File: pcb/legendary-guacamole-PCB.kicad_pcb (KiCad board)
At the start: 2 copper layers, 46 parts

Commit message: forget to commit
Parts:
- added REF**: XIAO-nRF52840-SMD, XIAO-nRF52840-SMD, F.Cu at (257.1, 59.7)
- B1, D1, D10, D11, D12, D13, D14, D15, D16, D17, D18, D19, D2, D20, D21, D22, D3, D4, D5, D6, D7, D8, D9, JST1, S1, S10, S11, S12, S13, S14, S15, S16, S17, S18, S19, S2, S20, S21, S22, S3, S4, S5, S6, S7, S8, S9: value ~ -> (none)
- moved B1 56.2 mm to (187.5, 57.4)
- moved JST1 54.3 mm to (193.8, 70.9)
- moved D1 48.1 mm to (71.0, 118.4)
- moved D10 48.1 mm to (128.0, 86.7)
- moved D11 48.1 mm to (128.0, 67.7)
- moved D12 48.1 mm to (147.0, 112.0)
- moved D13 48.1 mm to (147.0, 93.0)
- moved D14 48.1 mm to (147.0, 74.0)
- moved D15 48.1 mm to (166.0, 112.0)
- moved D16 48.1 mm to (166.0, 93.0)
- moved D17 48.1 mm to (166.0, 74.0)
- moved D2 48.1 mm to (71.0, 99.4)
- moved D4 48.1 mm to (90.0, 99.4)
- moved D5 48.1 mm to (90.0, 80.4)
- moved D6 48.1 mm to (109.0, 112.0)
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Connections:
- net /BAT_P renamed BAT_P
- net /GND renamed GND
- net /P0 renamed P0
- net /P1 renamed P1
- net /P10 renamed P10
- net /P2 renamed P2
- net /P3 renamed P3
- net /P4 renamed P4
- net /P5 renamed P5
- net /P6 renamed P6
- net /P7 renamed P7
- net /P8 renamed P8
- net /P9 renamed P9
- net /RST renamed RST
- net /index_bottom renamed index_bottom
- net /index_home renamed index_home
- net /index_top renamed index_top
- net /inner_bottom renamed inner_bottom
- net /inner_home renamed inner_home
- net /inner_top renamed inner_top
- net /middle_bottom renamed middle_bottom
- net /middle_home renamed middle_home
- net /middle_top renamed middle_top
- net /outer_bottom renamed outer_bottom
- net /outer_home renamed outer_home
- net /pinky_bottom renamed pinky_bottom
- net /pinky_home renamed pinky_home
- net /pinky_top renamed pinky_top
- net /ring_bottom renamed ring_bottom
- net /ring_home renamed ring_home
- net /ring_top renamed ring_top
- net /thumb_1_row_0 renamed thumb_1_row_0
- net /thumb_1_row_1 renamed thumb_1_row_1
- net /thumb_2_row_0 renamed thumb_2_row_0
- net /thumb_2_row_1 renamed thumb_2_row_1
- net /thumb_3_row_0 renamed thumb_3_row_0
- JST1 pad 11: (no net) -> JST1_1
- JST1 pad 12: (no net) -> JST1_2
- JST1 pad 21: (no net) -> JST1_1
- JST1 pad 22: (no net) -> JST1_2
- JST1 pad 31: (no net) -> JST1_1
- JST1 pad 32: (no net) -> JST1_2
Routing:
- net JST1_2: track 0.00 -> 3.60 mm
- net JST1_1: track 0.00 -> 3.60 mm

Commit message: update pcb with new key layout
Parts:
- added D23: , ComboDiode, F.Cu at (222.1, 143.9)
- added S23: , MX, F.Cu at (224.6, 139.6)
- moved REF** 264.0 mm to (0.00, 0.00)
- moved D18 103.7 mm to (195.0, 60.7), turned to 0 degrees
- moved S18 103.3 mm to (195.0, 55.7), turned to 0 degrees
- moved D12 58.6 mm to (157.0, 54.3)
- moved S12 58.6 mm to (157.0, 49.3)
- moved D15 52.3 mm to (176.0, 60.7)
- moved S15 52.3 mm to (176.0, 55.7)
- moved D3 52.3 mm to (100.0, 67.0)
- moved S3 52.3 mm to (100.0, 62.0)
- moved D6 46.1 mm to (119.0, 67.0)
- moved S6 46.1 mm to (119.0, 62.0)
- moved D9 46.1 mm to (138.0, 60.7)
- moved S9 46.1 mm to (138.0, 55.7)
- moved S22 42.8 mm to (207.7, 121.3), turned to -20 degrees
- moved S20 42.7 mm to (184.3, 116.8), turned to -10 degrees
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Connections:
- D10 pad 1: P7 -> P8
- D10 pad 2: middle_home -> middle_bottom
- D11 pad 1: P6 -> P7
- D11 pad 2: middle_top -> middle_home
- D12 pad 1: P8 -> P6
- D12 pad 2: index_bottom -> middle_top
- D13 pad 1: P7 -> P8
- D13 pad 2: index_home -> index_bottom
- D14 pad 1: P6 -> P7
- D14 pad 2: index_top -> index_home
- D15 pad 1: P8 -> P6
- D15 pad 2: inner_bottom -> index_top
- D16 pad 1: P7 -> P8
- D16 pad 2: inner_home -> inner_bottom
- D17 pad 1: P6 -> P7
- D17 pad 2: inner_top -> inner_home
- D18 pad 1: P10 -> P6
- D18 pad 2: thumb_1_row_0 -> inner_top
- D19 pad 1: P9 -> P10
- D19 pad 2: thumb_1_row_1 -> thumb_1_row_0
- D20 pad 1: P10 -> P9
- D20 pad 2: thumb_2_row_0 -> thumb_1_row_1
- D21 pad 1: P9 -> P10
- D21 pad 2: thumb_2_row_1 -> thumb_2_row_0
- D22 pad 1: P10 -> P9
- D22 pad 2: thumb_3_row_0 -> thumb_2_row_1
- D3 pad 1: P8 -> P6
- D3 pad 2: pinky_bottom -> outer_top
- D4 pad 1: P7 -> P8
- D4 pad 2: pinky_home -> pinky_bottom
- D5 pad 1: P6 -> P7
- D5 pad 2: pinky_top -> pinky_home
- D6 pad 1: P8 -> P6
- D6 pad 2: ring_bottom -> pinky_top
- D7 pad 1: P7 -> P8
- D7 pad 2: ring_home -> ring_bottom
- D8 pad 1: P6 -> P7
- D8 pad 2: ring_top -> ring_home
- D9 pad 1: P8 -> P6
- D9 pad 2: middle_bottom -> ring_top
- S10 pad 2: middle_home -> middle_bottom
- S11 pad 2: middle_top -> middle_home
- S12 pad 1: P4 -> P3
- S12 pad 2: index_bottom -> middle_top
- S13 pad 2: index_home -> index_bottom
- S14 pad 2: index_top -> index_home
- S15 pad 1: P5 -> P4
- S15 pad 2: inner_bottom -> index_top
- S16 pad 2: inner_home -> inner_bottom
- S17 pad 2: inner_top -> inner_home
- S18 pad 1: P3 -> P5
- S18 pad 2: thumb_1_row_0 -> inner_top
- S19 pad 2: thumb_1_row_1 -> thumb_1_row_0
- S20 pad 1: P4 -> P3
- S20 pad 2: thumb_2_row_0 -> thumb_1_row_1
- S21 pad 2: thumb_2_row_1 -> thumb_2_row_0
- S22 pad 1: P5 -> P4
- S22 pad 2: thumb_3_row_0 -> thumb_2_row_1
- S3 pad 1: P1 -> P0
- S3 pad 2: pinky_bottom -> outer_top
- S4 pad 2: pinky_home -> pinky_bottom
- S5 pad 2: pinky_top -> pinky_home
- S6 pad 1: P2 -> P1
- S6 pad 2: ring_bottom -> pinky_top
- S7 pad 2: ring_home -> ring_bottom
- S8 pad 2: ring_top -> ring_home
- S9 pad 1: P3 -> P2
- S9 pad 2: middle_bottom -> ring_top

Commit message: fix diff between updated pcb and schematic
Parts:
- moved REF** 230.0 mm to (220.4, 65.5)
- moved B1 43.6 mm to (236.2, 42.4)
- moved JST1 31.1 mm to (220.8, 43.0)
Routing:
- net P6: track 0.00 -> 3.60 mm
- net JST1_2: track 3.60 -> 0.00 mm
- net RST: track 0.00 -> 1.80 mm
- net JST1_1: track 3.60 -> 1.80 mm

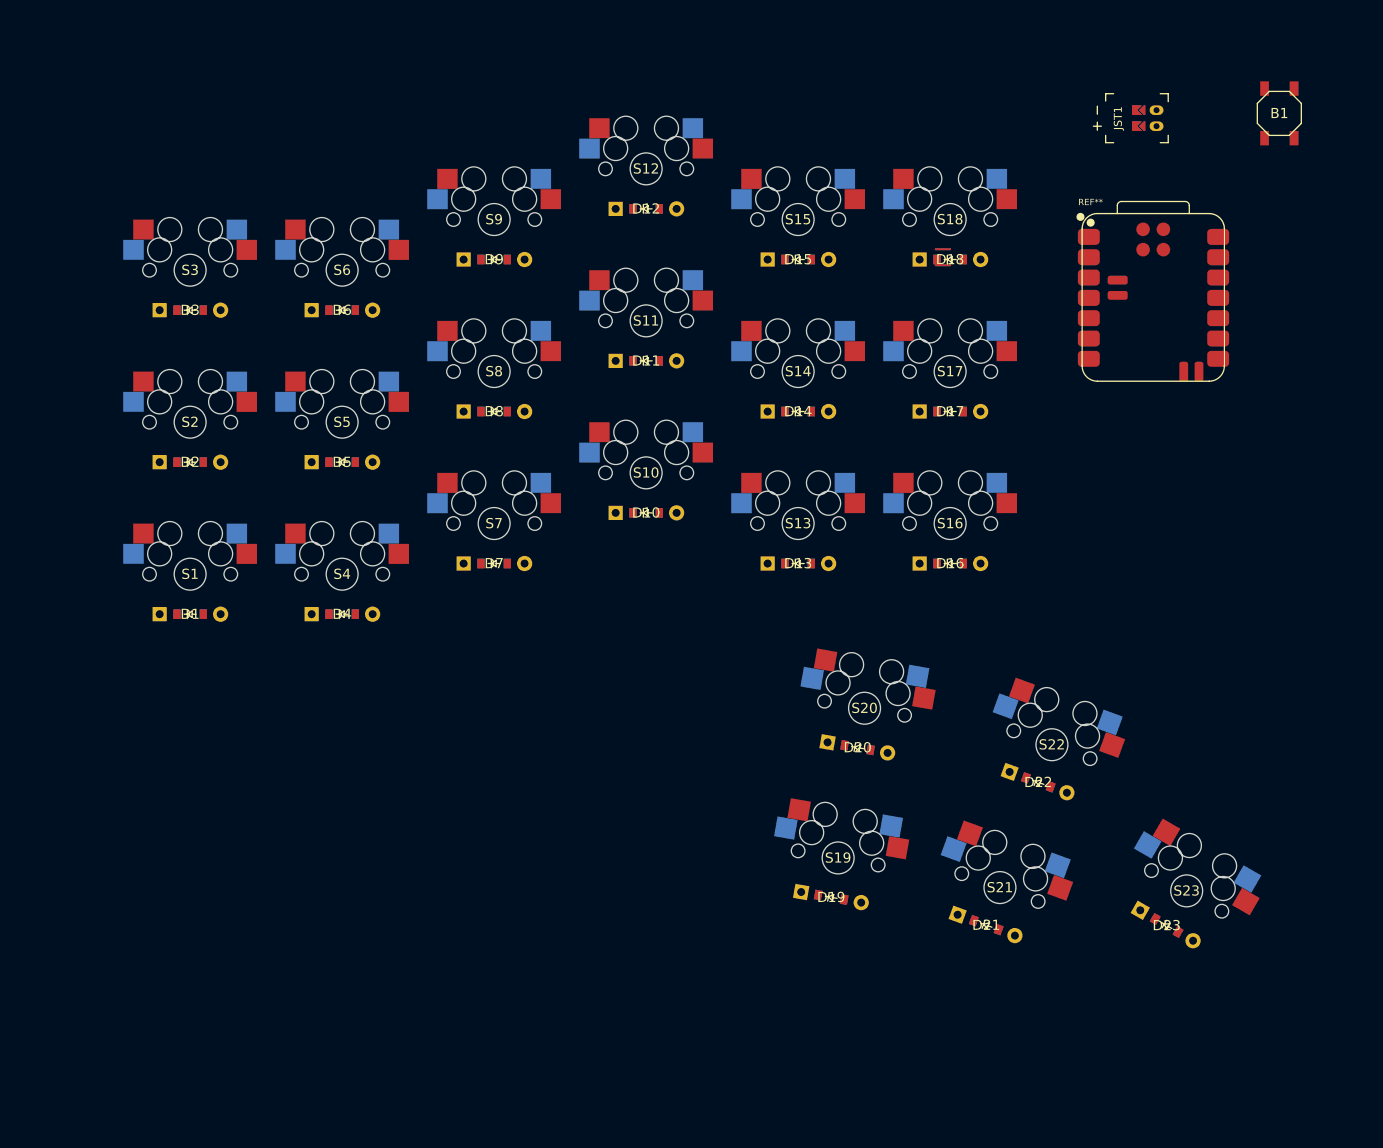
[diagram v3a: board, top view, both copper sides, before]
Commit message: finish pcb routing, generate fabrication file and bom
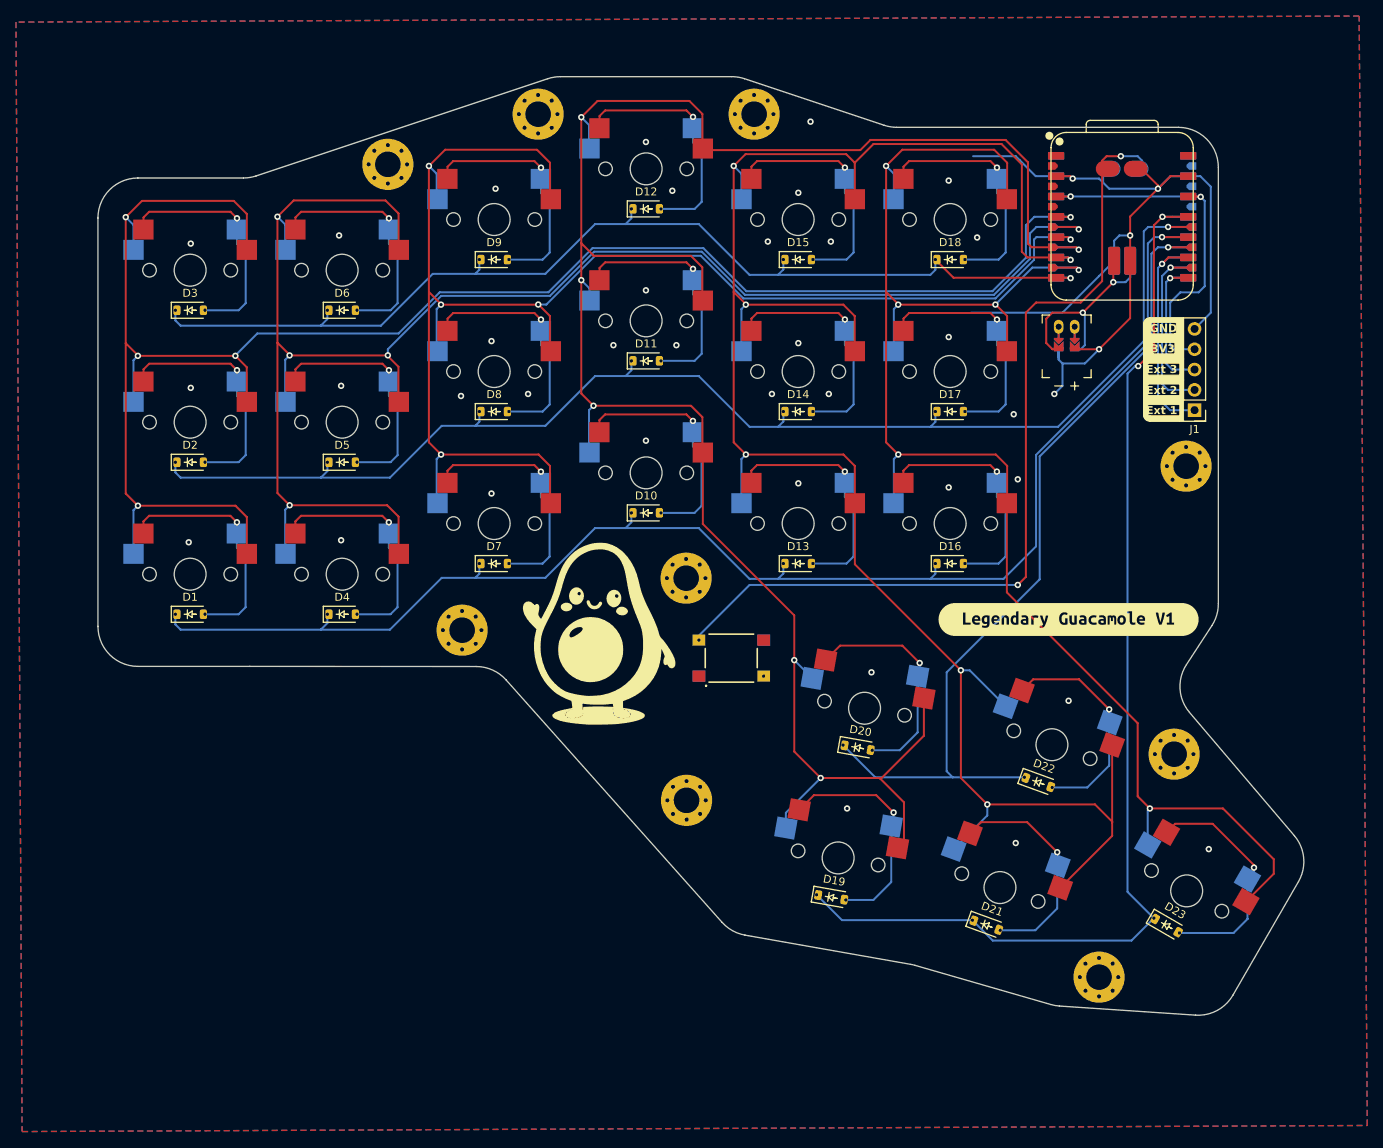
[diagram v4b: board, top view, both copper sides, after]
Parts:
- removed B1: , E73:SW_TACT_ALPS_SKQGABE010
- removed the REF** at (220.4, 65.5)
- added BTN1: EVPBT5A4A000, library:EVPBT5A4A000, F.Cu at (167.6, 110.5)
- added G***: LOGO, LOGO, F.Cu at (151.0, 106.9)
- added J1: ExtensionPort, Connector_PinHeader_2.54mm:PinHeader_1x05_P2.54mm_Vertical, F.Cu at (225.6, 79.5)
- added REF**: MountingHole_3.2mm_M3_Pad_Via, MountingHole:MountingHole_3.2mm_M3_Pad_Via, F.Cu at (124.7, 48.8)
- added REF**: MountingHole_3.2mm_M3_Pad_Via, MountingHole:MountingHole_3.2mm_M3_Pad_Via, F.Cu at (213.6, 150.4)
- added REF**: MountingHole_3.2mm_M3_Pad_Via, MountingHole:MountingHole_3.2mm_M3_Pad_Via, F.Cu at (162.0, 100.5)
- added REF**: MountingHole_3.2mm_M3_Pad_Via, MountingHole:MountingHole_3.2mm_M3_Pad_Via, F.Cu at (223.0, 122.5)
- added REF**: MountingHole_3.2mm_M3_Pad_Via, MountingHole:MountingHole_3.2mm_M3_Pad_Via, F.Cu at (143.5, 42.5)
- added REF**: MountingHole_3.2mm_M3_Pad_Via, MountingHole:MountingHole_3.2mm_M3_Pad_Via, F.Cu at (134.0, 107.0)
- added REF**: MountingHole_3.2mm_M3_Pad_Via, MountingHole:MountingHole_3.2mm_M3_Pad_Via, F.Cu at (224.5, 86.5)
- added REF**: MountingHole_3.2mm_M3_Pad_Via, MountingHole:MountingHole_3.2mm_M3_Pad_Via, F.Cu at (170.5, 42.5)
- added REF**: MountingHole_3.2mm_M3_Pad_Via, MountingHole:MountingHole_3.2mm_M3_Pad_Via, F.Cu at (162.1, 128.3)
- added U1: nRF52840 Plus, library:XIAO-nRF52840-Plus-SMD, F.Cu at (216.5, 55.3)
- added U1: nRF52840 Plus, library:XIAO-nRF52840-Plus-SMD, B.Cu at (216.5, 55.3)
- added kibuzzard-69750C78: G***, kibuzzard-69750C78, F.Cu at (209.8, 105.7)
- D1, D10, D11, D12, D13, D14, D15, D16, D17, D18, D19, D2, D20, D21, D22, D23, D3, D4, D5, D6, D7, D8, D9: footprint ComboDiode -> library:ComboDiode
- JST1: footprint ceoloide:battery_connector_jst_ph_2 -> library:JST; moved to B.Cu
- S1, S10, S11, S12, S13, S14, S15, S16, S17, S18, S19, S2, S20, S21, S22, S23, S3, S4, S5, S6, S7, S8, S9: footprint MX -> library:SwitchSocket
- moved JST1 30.6 mm to (209.5, 71.4), turned to 180 degrees
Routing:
- net P3: track 0.00 -> 262.1 mm, vias 0 -> 6
- net P4: track 0.00 -> 252.7 mm, vias 0 -> 6
- net P0: track 0.00 -> 234.7 mm, vias 0 -> 5
- net P1: track 0.00 -> 217.6 mm, vias 0 -> 5
- net P5: track 0.00 -> 205.4 mm, vias 0 -> 6
- net P2: track 0.00 -> 192.4 mm, vias 0 -> 5
- net P8: track 0.00 -> 181.8 mm, vias 0 -> 1
- net P7: track 0.00 -> 168.5 mm, vias 0 -> 1
- net P10: track 0.00 -> 143.2 mm, vias 0 -> 2
- net P6: track 3.60 -> 134.3 mm, vias 0 -> 1
- net GND: track 0.00 -> 127.7 mm, vias 0 -> 41
- net Net-(BTN1-A): track 0.00 -> 110.2 mm, vias 0 -> 2
- net P9: track 0.00 -> 108.9 mm, vias 0 -> 1
- net +3V3: track 0.00 -> 47.1 mm, vias 0 -> 2
- net ring_home: track 0.00 -> 30.3 mm, vias 0 -> 1
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- added copper zone on B.Cu, net GND
- added copper zone on F.Cu, net GND
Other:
- board outline added: 150.7 x 117.3 mm
- board text added: "3V3"
- board text added: "Ext 1"
- board text added: "Ext 2"
- board text added: "Ext 3"
- board text added: "GND"

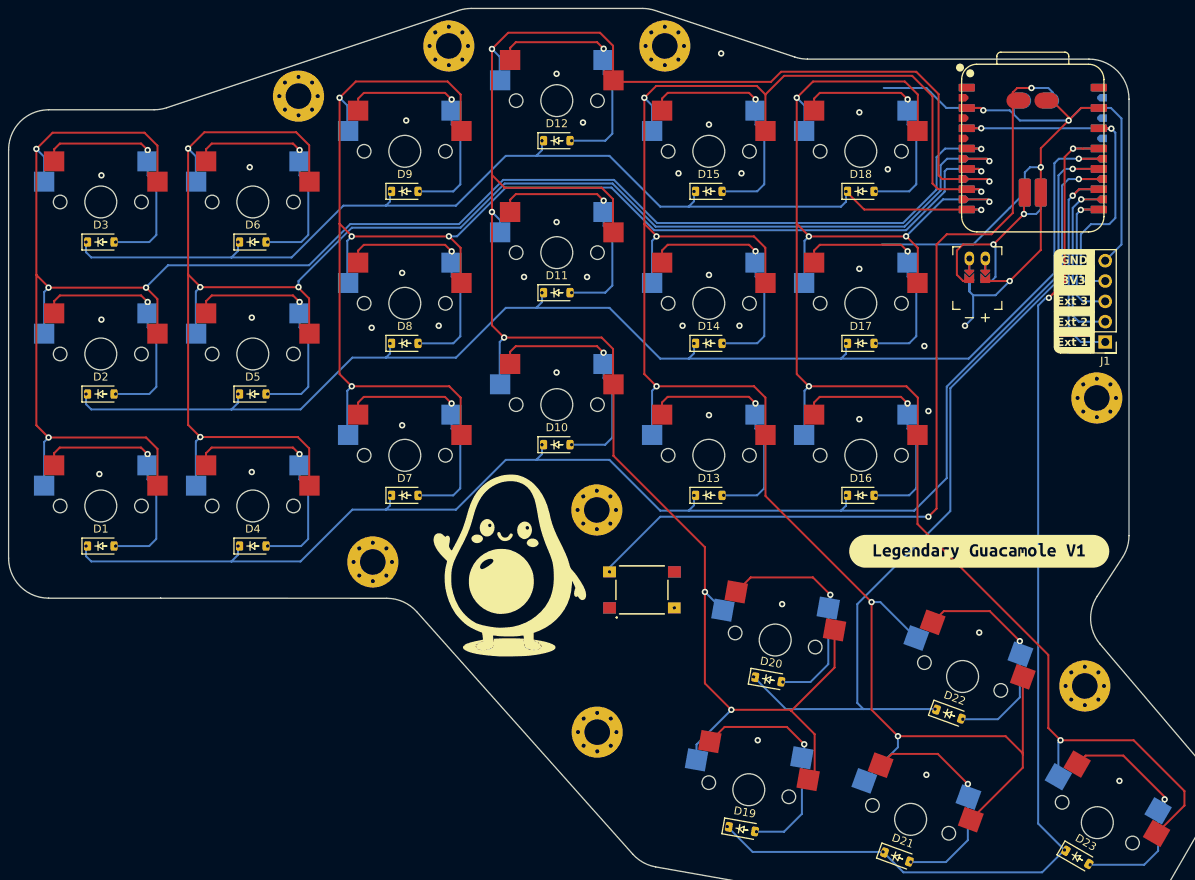
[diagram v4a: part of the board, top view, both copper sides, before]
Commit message: fix pcb (update sw footprint), start case design
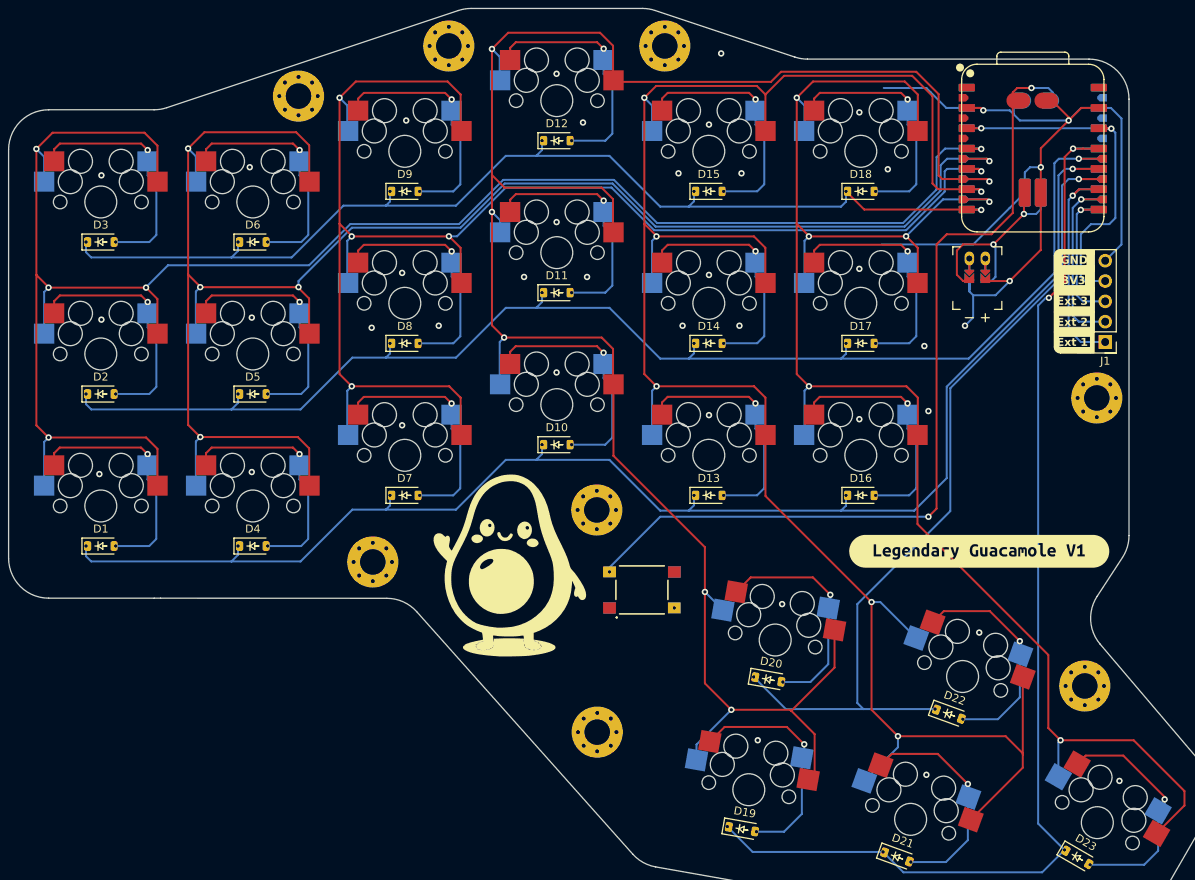
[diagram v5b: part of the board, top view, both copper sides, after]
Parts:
- added G***: LOGO, LOGO, B.Cu at (152.4, 109.7)
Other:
- outline, holes or cut-outs redrawn
